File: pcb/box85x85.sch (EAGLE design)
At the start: 28 parts, among them K1 ZF112, K2 ZF112, K3 ZF112, U1 LM1117-3.3, X1 MKDSN1,5/2-5,08, X2 MKDSN1,5/2-5,08, X3 MKDSN1,5/2-5,08, X4 MKDSN1,5/2-5,08

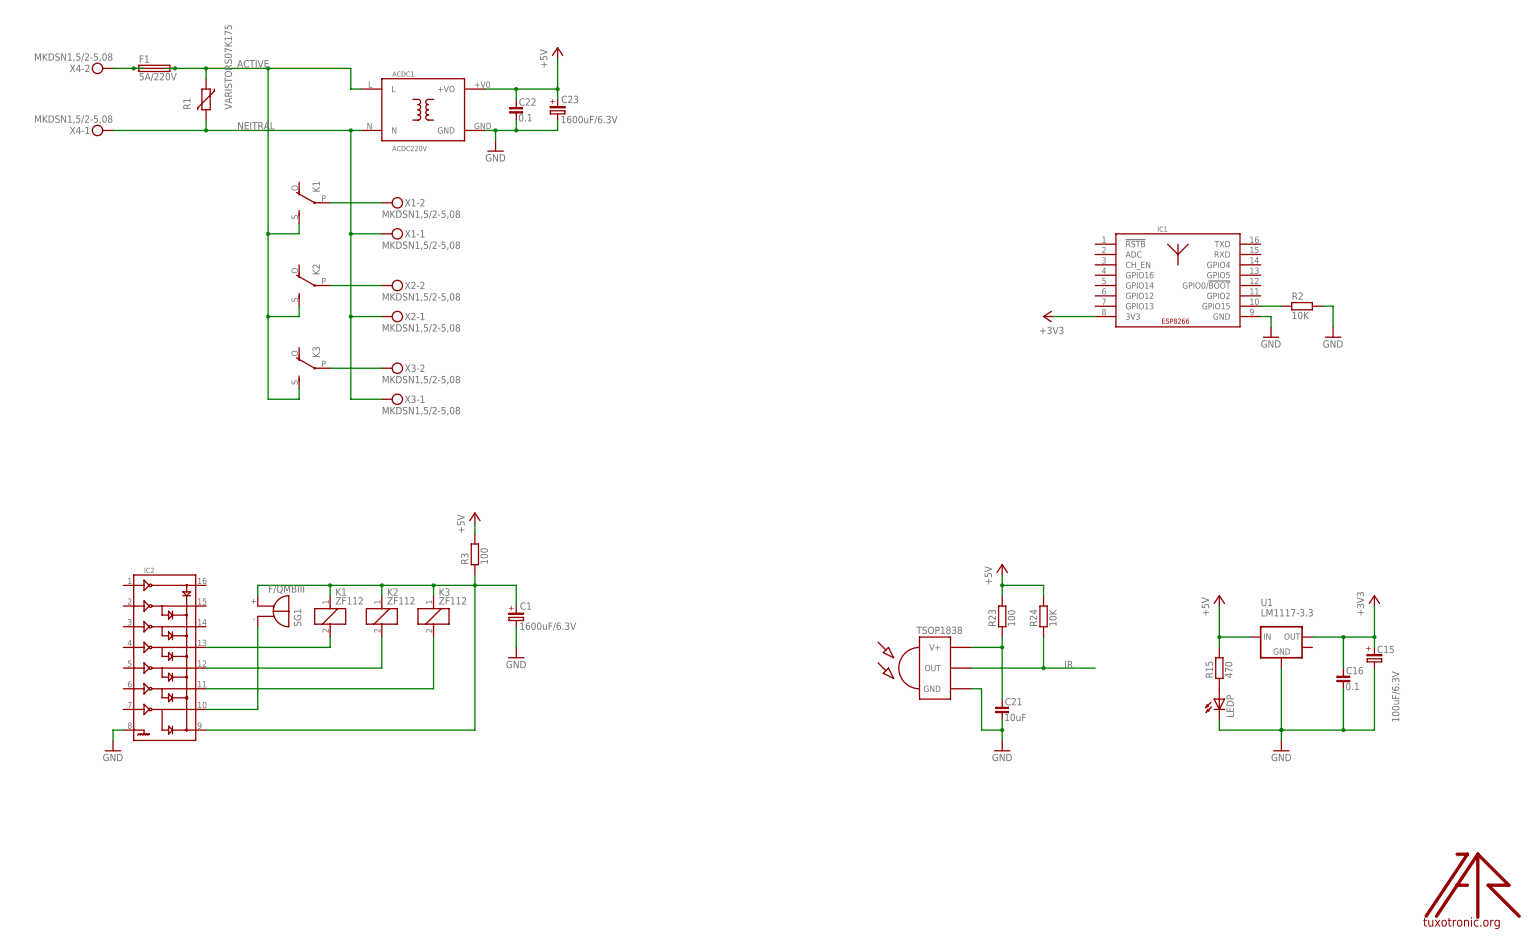
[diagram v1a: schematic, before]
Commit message: pcb in progress.  connect relays
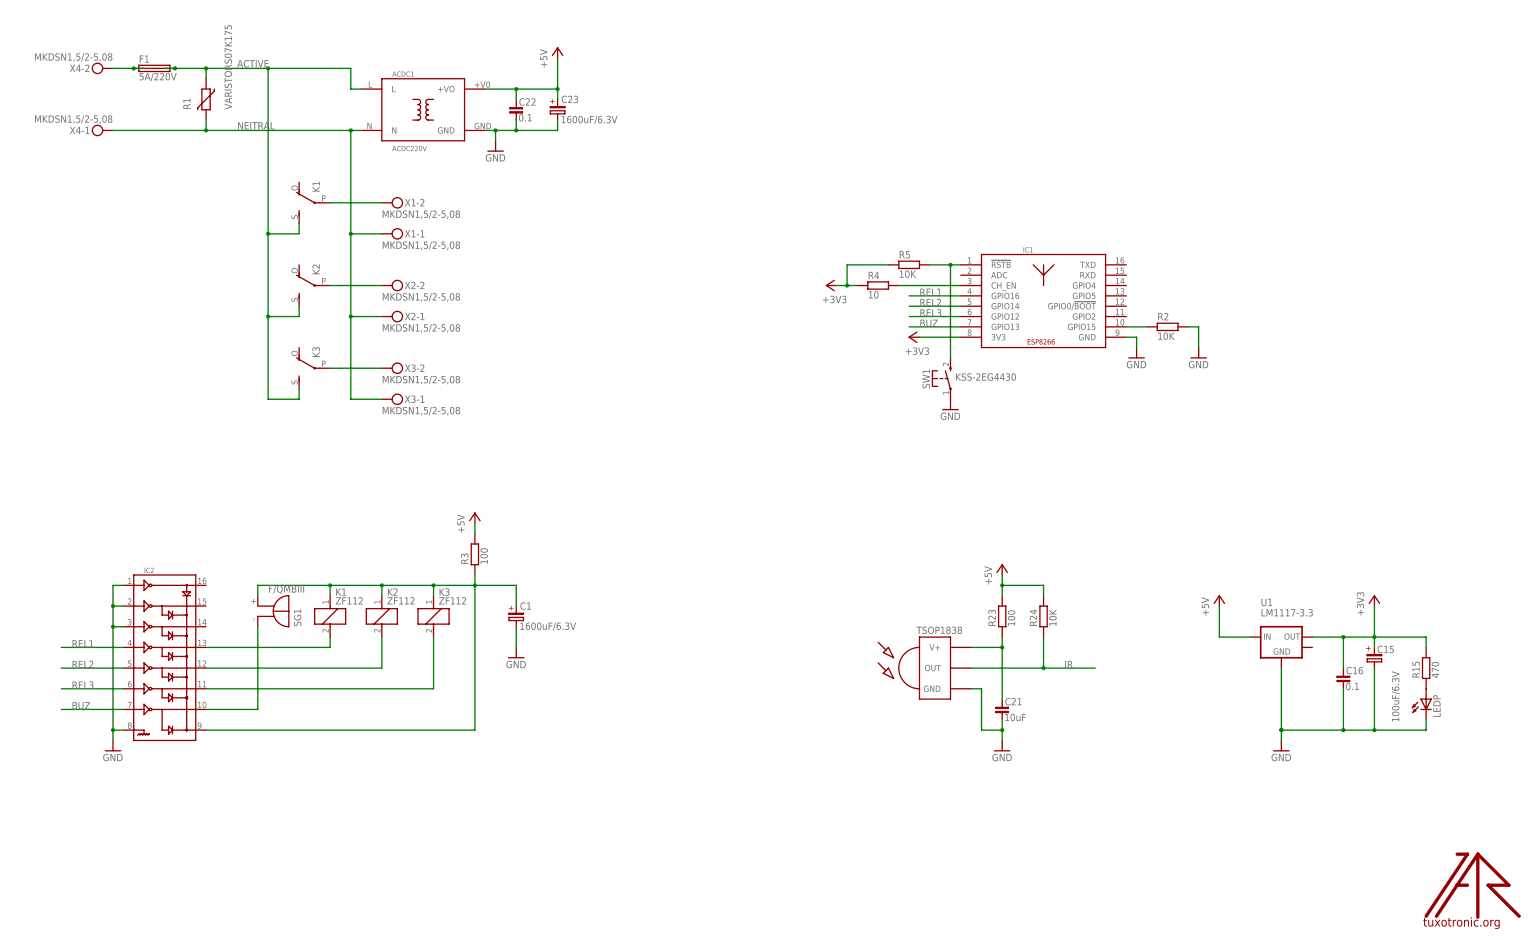
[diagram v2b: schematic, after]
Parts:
- added R4: 10, rc-master-smd:R_0603
- added R5: 10K, rc-master-smd:R_0603
- added SW1: KSS-2EG4430, buttons:KSS-2EG4430
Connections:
- new net BUZ: IC1.GPIO13, IC2.7
- new net N$15: IC1.CH_EN, R4.2
- new net N$16: IC1.!RSTB, R5.2, SW1.S
- new net REL1: IC1.GPIO16, IC2.4
- new net REL2: IC1.GPIO14, IC2.5
- new net REL3: IC1.GPIO12, IC2.6
- net +3V3: now also R15.2, R4.1, R5.1
- net +5V: no longer R15.2
- net GND: now also IC2.1, IC2.2, IC2.3, SW1.P
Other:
- moved on the sheet: IC1, LEDP, R15, R2
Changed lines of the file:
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@@
 <part name="IC2" library="transistor-arrays" deviceset="ULN2003" device="D"/>
 <part name="GND8" library="supply1" deviceset="GND" device=""/>
+<part name="R4" library="rc-master-smd" deviceset="R_" device="0603" value="10"/>
+<part name="+3V2" library="supply1" deviceset="+3V3" device=""/>
+<part name="SW1" library="buttons" deviceset="KSS-2EG4430" device=""/>
+<part name="GND5" library="rs485" deviceset="GND" device=""/>
+<part name="R5" library="rc-master-smd" deviceset="R_" device="0603" value="10K"/>
 </parts>
 <sheets>
@@
 <attribute name="VALUE" x="344.678" y="83.058" size="1.778" layer="96" rot="R270"/>
 </instance>
-<instance part="R15" gate="G$1" x="302.26" y="83.82" rot="R90"/>
-<instance part="LEDP" gate="G$1" x="302.26" y="76.2"/>
+<instance part="R15" gate="G$1" x="353.06" y="83.82" rot="R90"/>
+<instance part="LEDP" gate="G$1" x="353.06" y="76.2"/>
 <instance part="P+7" gate="1" x="302.26" y="101.6"/>
 <instance part="IR1" gate="G$1" x="233.68" y="83.82"/>
@@
 <instance part="K3" gate="1" x="109.22" y="96.52"/>
 <instance part="K3" gate="2" x="81.28" y="157.48" rot="R90"/>
-<instance part="IC1" gate="G$1" x="292.1" y="180.34"/>
-<instance part="GND2" gate="1" x="314.96" y="165.1"/>
-<instance part="+3V1" gate="G$1" x="259.08" y="170.18" rot="R90"/>
-<instance part="R2" gate="G$1" x="322.58" y="172.72"/>
-<instance part="GND3" gate="1" x="330.2" y="165.1"/>
+<instance part="IC1" gate="G$1" x="259.08" y="175.26"/>
+<instance part="GND2" gate="1" x="281.94" y="160.02"/>
+<instance part="+3V1" gate="G$1" x="226.06" y="165.1" rot="R90"/>
+<instance part="R2" gate="G$1" x="289.56" y="167.64"/>
+<instance part="GND3" gate="1" x="297.18" y="160.02"/>
 <instance part="P+1" gate="1" x="119.38" y="121.92"/>
 <instance part="C1" gate="G$1" x="129.54" y="96.52"/>
@@
 <instance part="IC2" gate="G$1" x="43.18" y="86.36"/>
 <instance part="GND8" gate="1" x="30.48" y="63.5"/>
+<instance part="R4" gate="G$1" x="218.44" y="177.8"/>
+<instance part="+3V2" gate="G$1" x="205.74" y="177.8" rot="R90"/>
+<instance part="SW1" gate="G$1" x="236.22" y="154.94" smashed="yes" rot="R90">
+<attribute name="NAME" x="231.14" y="152.4" size="1.778" layer="95" rot="R90"/>
+<attribute name="VALUE" x="237.363" y="154.432" size="1.778" layer="96"/>
+</instance>
+<instance part="GND5" gate="1" x="236.22" y="147.32"/>
+<instance part="R5" gate="G$1" x="226.06" y="182.88"/>
 </instances>
 <busses>
@@
 <wire x1="317.5" y1="83.82" x2="317.5" y2="68.58" width="0.1524" layer="91"/>
 <wire x1="317.5" y1="66.04" x2="317.5" y2="68.58" width="0.1524" layer="91"/>
-<wire x1="302.26" y1="68.58" x2="302.26" y2="71.12" width="0.1524" layer="91"/>
-<wire x1="302.26" y1="68.58" x2="317.5" y2="68.58" width="0.1524" layer="91"/>
 <junction x="332.74" y="68.58"/>
 <junction x="317.5" y="68.58"/>
@@
 <pinref part="GND32" gate="1" pin="GND"/>
 <pinref part="LEDP" gate="G$1" pin="C"/>
+<wire x1="340.36" y1="68.58" x2="353.06" y2="68.58" width="0.1524" layer="91"/>
+<wire x1="353.06" y1="68.58" x2="353.06" y2="71.12" width="0.1524" layer="91"/>
+<junction x="340.36" y="68.58"/>
 </segment>
 <segment>
@@
 <pinref part="IC1" gate="G$1" pin="GND"/>
 <pinref part="GND2" gate="1" pin="GND"/>
-<wire x1="312.42" y1="170.18" x2="314.96" y2="170.18" width="0.1524" layer="91"/>
-<wire x1="314.96" y1="170.18" x2="314.96" y2="167.64" width="0.1524" layer="91"/>
+<wire x1="279.4" y1="165.1" x2="281.94" y2="165.1" width="0.1524" layer="91"/>
+<wire x1="281.94" y1="165.1" x2="281.94" y2="162.56" width="0.1524" layer="91"/>
 </segment>
 <segment>
 <pinref part="R2" gate="G$1" pin="2"/>
 <pinref part="GND3" gate="1" pin="GND"/>
-<wire x1="327.66" y1="172.72" x2="330.2" y2="172.72" width="0.1524" layer="91"/>
-<wire x1="330.2" y1="172.72" x2="330.2" y2="167.64" width="0.1524" layer="91"/>
+<wire x1="294.64" y1="167.64" x2="297.18" y2="167.64" width="0.1524" layer="91"/>
+<wire x1="297.18" y1="167.64" x2="297.18" y2="162.56" width="0.1524" layer="91"/>
 </segment>
 <segment>
@@
 <wire x1="33.02" y1="68.58" x2="30.48" y2="68.58" width="0.1524" layer="91"/>
 <wire x1="30.48" y1="68.58" x2="30.48" y2="66.04" width="0.1524" layer="91"/>
+<pinref part="IC2" gate="G$1" pin="1"/>
+<wire x1="33.02" y1="104.14" x2="30.48" y2="104.14" width="0.1524" layer="91"/>
+<wire x1="30.48" y1="104.14" x2="30.48" y2="99.06" width="0.1524" layer="91"/>
+<junction x="30.48" y="68.58"/>
+<pinref part="IC2" gate="G$1" pin="2"/>
+<wire x1="30.48" y1="99.06" x2="30.48" y2="93.98" width="0.1524" layer="91"/>
+<wire x1="30.48" y1="93.98" x2="30.48" y2="68.58" width="0.1524" layer="91"/>
+<wire x1="33.02" y1="99.06" x2="30.48" y2="99.06" width="0.1524" layer="91"/>
+<junction x="30.48" y="99.06"/>
+<pinref part="IC2" gate="G$1" pin="3"/>
+<wire x1="33.02" y1="93.98" x2="30.48" y2="93.98" width="0.1524" layer="91"/>
+<junction x="30.48" y="93.98"/>
+</segment>
+<segment>
+<pinref part="SW1" gate="G$1" pin="P"/>
+<pinref part="GND5" gate="1" pin="GND"/>
 </segment>
 </net>
@@
 <pinref part="C16" gate="G$1" pin="1"/>
 <pinref part="C15" gate="G$1" pin="+"/>
+<pinref part="R15" gate="G$1" pin="2"/>
+<wire x1="340.36" y1="91.44" x2="353.06" y2="91.44" width="0.1524" layer="91"/>
+<wire x1="353.06" y1="91.44" x2="353.06" y2="88.9" width="0.1524" layer="91"/>
 </segment>
 <segment>
 <pinref part="+3V1" gate="G$1" pin="+3V3"/>
 <pinref part="IC1" gate="G$1" pin="3V3"/>
-<wire x1="261.62" y1="170.18" x2="271.78" y2="170.18" width="0.1524" layer="91"/>
+<wire x1="228.6" y1="165.1" x2="238.76" y2="165.1" width="0.1524" layer="91"/>
+</segment>
+<segment>
+<pinref part="+3V2" gate="G$1" pin="+3V3"/>
+<pinref part="R4" gate="G$1" pin="1"/>
+<wire x1="208.28" y1="177.8" x2="210.82" y2="177.8" width="0.1524" layer="91"/>
+<pinref part="R5" gate="G$1" pin="1"/>
+<wire x1="210.82" y1="177.8" x2="213.36" y2="177.8" width="0.1524" layer="91"/>
+<wire x1="220.98" y1="182.88" x2="210.82" y2="182.88" width="0.1524" layer="91"/>
+<wire x1="210.82" y1="182.88" x2="210.82" y2="177.8" width="0.1524" layer="91"/>
+<junction x="210.82" y="177.8"/>
 </segment>
 </net>
@@
 <segment>
 <wire x1="302.26" y1="91.44" x2="309.88" y2="91.44" width="0.1524" layer="91"/>
-<wire x1="302.26" y1="88.9" x2="302.26" y2="91.44" width="0.1524" layer="91"/>
 <wire x1="302.26" y1="91.44" x2="302.26" y2="99.06" width="0.1524" layer="91"/>
-<junction x="302.26" y="91.44"/>
 <pinref part="U1" gate="G$1" pin="IN"/>
-<pinref part="R15" gate="G$1" pin="2"/>
 <pinref part="P+7" gate="1" pin="+5V"/>
 </segment>
@@
 <pinref part="IC1" gate="G$1" pin="GPIO15"/>
 <pinref part="R2" gate="G$1" pin="1"/>
-<wire x1="312.42" y1="172.72" x2="317.5" y2="172.72" width="0.1524" layer="91"/>
+<wire x1="279.4" y1="167.64" x2="284.48" y2="167.64" width="0.1524" layer="91"/>
 </segment>
 </net>
@@
 </segment>
 </net>
+<net name="REL1" class="0">
+<segment>
+<pinref part="IC2" gate="G$1" pin="4"/>
+<wire x1="33.02" y1="88.9" x2="17.78" y2="88.9" width="0.1524" layer="91"/>
+<label x="20.32" y="88.9" size="1.778" layer="95"/>
+</segment>
+<segment>
+<pinref part="IC1" gate="G$1" pin="GPIO16"/>
+<wire x1="238.76" y1="175.26" x2="226.06" y2="175.26" width="0.1524" layer="91"/>
+<label x="228.6" y="175.26" size="1.778" layer="95"/>
+</segment>
+</net>
+<net name="REL2" class="0">
+<segment>
+<pinref part="IC2" gate="G$1" pin="5"/>
+<wire x1="33.02" y1="83.82" x2="17.78" y2="83.82" width="0.1524" layer="91"/>
+<label x="20.32" y="83.82" size="1.778" layer="95"/>
+</segment>
+<segment>
+<pinref part="IC1" gate="G$1" pin="GPIO14"/>
+<wire x1="238.76" y1="172.72" x2="226.06" y2="172.72" width="0.1524" layer="91"/>
+<label x="228.6" y="172.72" size="1.778" layer="95"/>
+</segment>
+</net>
+<net name="REL3" class="0">
+<segment>
+<pinref part="IC2" gate="G$1" pin="6"/>
+<wire x1="33.02" y1="78.74" x2="17.78" y2="78.74" width="0.1524" layer="91"/>
+<label x="20.32" y="78.74" size="1.778" layer="95"/>
+</segment>
+<segment>
+<pinref part="IC1" gate="G$1" pin="GPIO12"/>
+<wire x1="238.76" y1="170.18" x2="226.06" y2="170.18" width="0.1524" layer="91"/>
+<label x="228.6" y="170.18" size="1.778" layer="95"/>
+</segment>
+</net>
+<net name="BUZ" class="0">
+<segment>
+<pinref part="IC2" gate="G$1" pin="7"/>
+<wire x1="33.02" y1="73.66" x2="17.78" y2="73.66" width="0.1524" layer="91"/>
+<label x="20.32" y="73.66" size="1.778" layer="95"/>
+</segment>
+<segment>
+<pinref part="IC1" gate="G$1" pin="GPIO13"/>
+<wire x1="238.76" y1="167.64" x2="226.06" y2="167.64" width="0.1524" layer="91"/>
+<label x="228.6" y="167.64" size="1.778" layer="95"/>
+</segment>
+</net>
+<net name="N$16" class="0">
+<segment>
+<pinref part="IC1" gate="G$1" pin="!RSTB"/>
+<pinref part="SW1" gate="G$1" pin="S"/>
+<wire x1="238.76" y1="182.88" x2="236.22" y2="182.88" width="0.1524" layer="91"/>
+<wire x1="236.22" y1="182.88" x2="236.22" y2="160.02" width="0.1524" layer="91"/>
+<pinref part="R5" gate="G$1" pin="2"/>
+<wire x1="231.14" y1="182.88" x2="236.22" y2="182.88" width="0.1524" layer="91"/>
+<junction x="236.22" y="182.88"/>
+</segment>
+</net>
+<net name="N$15" class="0">
+<segment>
+<pinref part="R4" gate="G$1" pin="2"/>
+<pinref part="IC1" gate="G$1" pin="CH_EN"/>
+<wire x1="223.52" y1="177.8" x2="238.76" y2="177.8" width="0.1524" layer="91"/>
+</segment>
+</net>

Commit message: PCB ready for LUT
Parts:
- added JP1: (no value), pinhead-fixdrills:PINHD-2X5_2.54
- added LED1, LED2, LED3: (no value), led:LED3MM
- added R10, R9: 10K, rc-master-smd:R_0805
- added R6, R7, R8: 470, rc-master-smd:R_0805
- C1, C23: device rc-master:CP_E-050X100 -> rc-master:CP_E-035X080
- C21: device rc-master-smd:C_0603 -> rc-master-smd:C_0805
- LEDP: device led:LEDCHIPLED_0805 -> led:LED3MM
- R15, R2, R23, R24, R4, R5: device rc-master-smd:R_0603 -> rc-master-smd:R_0805
- R3: value 100 -> 10
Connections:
- removed net N$13: C1.+, IC2.9, K11.1, K21.1, K31.1, R3.1, SG1.-
- new net +5V_FILTER: C1.+, IC2.9, K11.1, K21.1, K31.1, LED1.A, LED2.A, LED3.A, R3.1, SG1.-
- new net ADC: IC1.ADC, JP1.7
- new net GPIO0: IC1.GPIO0/!BOOT, JP1.5, R9.1
- new net GPIO15: IC1.GPIO15, JP1.4, R2.1
- new net GPIO2: IC1.GPIO2, JP1.6, R10.1
- new net GPIO5: IC1.GPIO5, JP1.8
- new net N$17: LED2.C, R7.1
- new net N$18: LED3.C, R8.1
- new net RXD: IC1.RXD, JP1.10
- new net TXD: IC1.TXD, JP1.9
- net +3V3: now also JP1.2, R10.2, R24.2, R9.2, U1.MASS
- net +5V: now also JP1.1; no longer R24.2
- net GND: now also JP1.3
- net IR: now also IC1.GPIO4
- net N$11: now also LED1.C, R6.1; no longer IC1.GPIO15, R2.1
- net N$12: now also R8.2
- net N$5: now also R6.2
- net N$6: now also R7.2
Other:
- moved on the sheet: IC1, R2, R4, R5, SW1
